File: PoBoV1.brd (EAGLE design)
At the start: 142.2 x 64.8 mm, 80 parts, among them IC1 INA232, Q1 IPZ40N04S5L-4R8, Q2 IPZ40N04S5L-4R8, U1 TPS55288RPMR, X1 +Vin, X18 OUT, X19 ADDRSEL, X3 SDA, X4 SCL, X5 VOUT/EXT, X6 FB SEL, X7 EN SEL, X8 MODE SEL

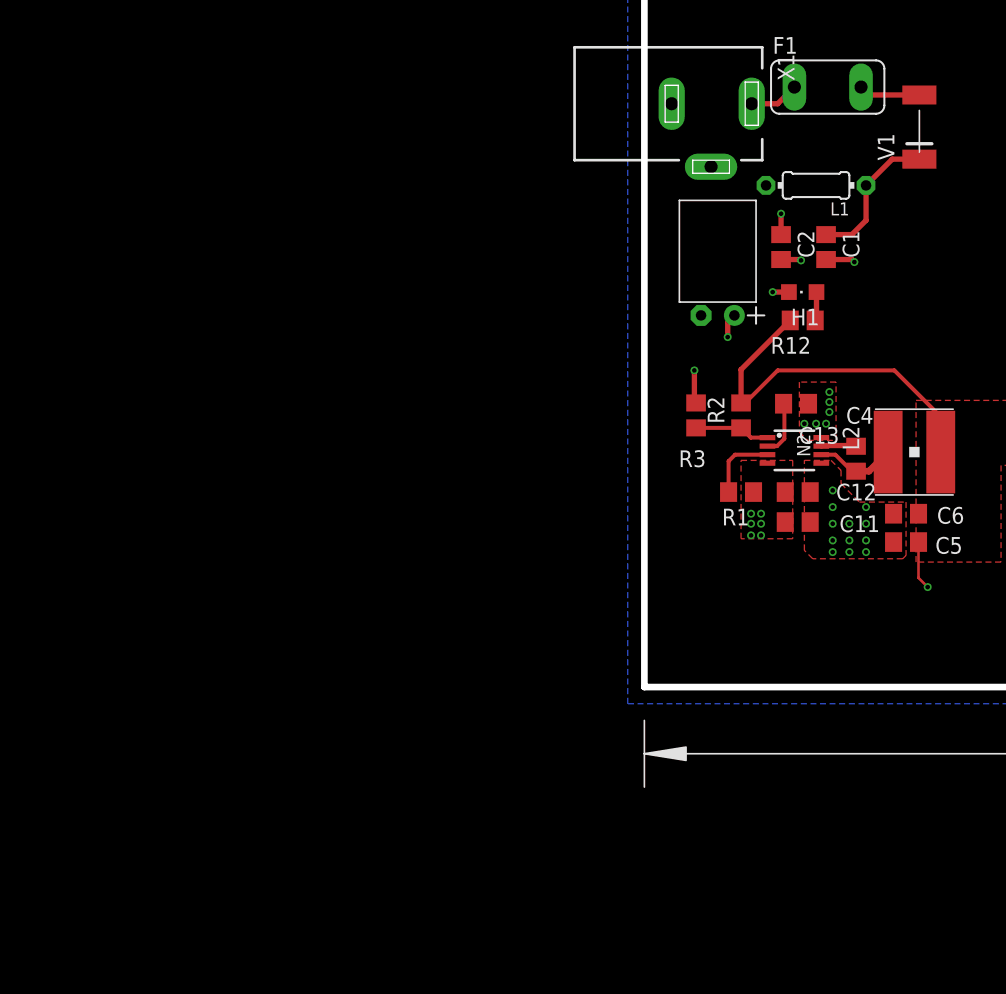
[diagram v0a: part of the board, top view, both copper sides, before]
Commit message: Made some traces thiccer and added bananaplug
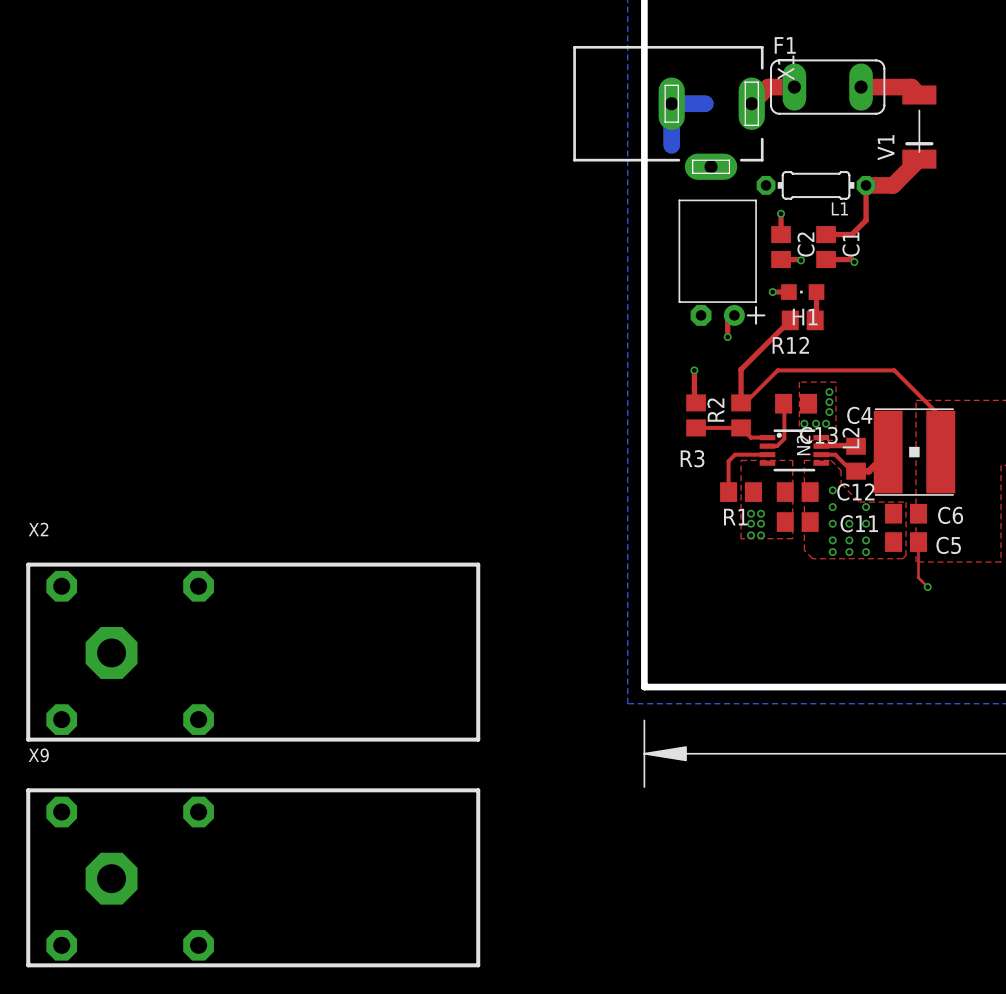
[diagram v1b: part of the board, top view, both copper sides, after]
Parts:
- added X2: BANANAJACKBANANAJACK-BLACK, con_PoeD:BANANAJACK
- added X9: BANANAJACKBANANAJACK-RED, con_PoeD:BANANAJACK
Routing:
- net PGND: track 11.5 -> 17.3 mm
- net VCC: track 7.47 -> 9.60 mm
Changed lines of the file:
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@@
 <setting verticaltext="up"/>
 </settings>
-<grid distance="0.1" unitdist="mm" unit="mm" style="lines" multiple="1" display="no" altdistance="5" altunitdist="mil" altunit="mil"/>
+<grid distance="3.93700787" unitdist="mil" unit="mil" style="lines" multiple="1" display="no" altdistance="5" altunitdist="mil" altunit="mil"/>
 <layers>
 <layer number="1" name="Top" color="4" fill="1" visible="yes" active="yes"/>
@@
 <layer number="23" name="tOrigins" color="15" fill="1" visible="yes" active="yes"/>
 <layer number="24" name="bOrigins" color="15" fill="1" visible="yes" active="yes"/>
-<layer number="25" name="tNames" color="7" fill="1" visible="no" active="yes"/>
-<layer number="26" name="bNames" color="7" fill="1" visible="no" active="yes"/>
-<layer number="27" name="tValues" color="7" fill="1" visible="no" active="yes"/>
-<layer number="28" name="bValues" color="7" fill="1" visible="no" active="yes"/>
+<layer number="25" name="tNames" color="7" fill="1" visible="yes" active="yes"/>
+<layer number="26" name="bNames" color="7" fill="1" visible="yes" active="yes"/>
+<layer number="27" name="tValues" color="7" fill="1" visible="yes" active="yes"/>
+<layer number="28" name="bValues" color="7" fill="1" visible="yes" active="yes"/>
 <layer number="29" name="tStop" color="18" fill="3" visible="no" active="yes"/>
 <layer number="30" name="bStop" color="18" fill="5" visible="no" active="yes"/>
@@
 </layers>
 <board>
-<fusionsync huburn="a.YnVzaW5lc3M6aHRsc2FsemJ1cmc0OTQ" projecturn="a.YnVzaW5lc3M6aHRsc2FsemJ1cmc0OTQjRDIwMjIwOTIyNTU5MzQ0OTgx" f3durn="urn:adsk.wipprod:dm.lineage:csbvKVBoTdiHW0NaQc5oYw" pcbguid="" lastpulledtime="" lastsyncedchangeguid="" latestrevisionid="9871288b-a15c-4ba2-ae32-102903a1a666" lastsyncedrevisionid="9871288b-a15c-4ba2-ae32-102903a1a666" lastboardhashguid="696e8a89-2363-cbe4-064f-950dd3bf885a" lastpushedtime="2024-12-28T18:32:02Z" linktopcb3d="true"/>
+<fusionsync huburn="a.YnVzaW5lc3M6aHRsc2FsemJ1cmc0OTQ" projecturn="a.YnVzaW5lc3M6aHRsc2FsemJ1cmc0OTQjRDIwMjIwOTIyNTU5MzQ0OTgx" f3durn="urn:adsk.wipprod:dm.lineage:csbvKVBoTdiHW0NaQc5oYw" pcbguid="" lastpulledtime="" lastsyncedchangeguid="" latestrevisionid="9871288b-a15c-4ba2-ae32-102903a1a666" lastsyncedrevisionid="9871288b-a15c-4ba2-ae32-102903a1a666" lastboardhashguid="696e8a89-2363-cbe4-064f-950dd3bf885a" lastpushedtime="2024-12-28T18:32:02Z" linktopcb3d="false"/>
 <plain>
 <wire x1="0" y1="0" x2="0" y2="64.77" width="0.508" layer="20"/>
@@
 <element name="FABRICATION" library="fabrication" package="FABRIACTION" value="" x="39.12" y="-10" smashed="yes"/>
 <element name="BOM" library="fabrication" package="BOM" value="" x="0.15" y="-0.15" smashed="yes"/>
+<element name="X2" library="con_PoeD" library_urn="urn:adsk.eagle:library:37347325" package="BANANAJACK" package3d_urn="urn:adsk.eagle:package:40115465/7" value="BANANAJACKBANANAJACK-BLACK" x="-40.6" y="2.6" smashed="yes">
+<attribute name="NAME" x="-46.95" y="11.49" size="1.016" layer="25"/>
+<attribute name="VALUE" x="-46.95" y="10.22" size="0.8128" layer="27"/>
+</element>
+<element name="X9" library="con_PoeD" library_urn="urn:adsk.eagle:library:37347325" package="BANANAJACK" package3d_urn="urn:adsk.eagle:package:40115465/7" value="BANANAJACKBANANAJACK-RED" x="-40.6" y="-14.6" smashed="yes">
+<attribute name="NAME" x="-46.95" y="-5.71" size="1.016" layer="25"/>
+<attribute name="VALUE" x="-46.95" y="-6.98" size="0.8128" layer="27"/>
+</element>
 </elements>
 <signals>
@@
 <wire x1="106.553" y1="10.988" x2="105.664" y2="10.099" width="0.2032" layer="1"/>
 <wire x1="105.664" y1="10.099" x2="105.664" y2="9.398" width="0.2032" layer="1"/>
-<polygon width="0.1524" layer="2">
+<polygon width="0.1524" layer="2" isolate="0.3048">
 <vertex x="-1.27" y="71.12"/>
 <vertex x="147.32" y="71.12"/>
@@
 <contactref element="C10" pad="2"/>
 <contactref element="H1" pad="C"/>
-<polygon width="0.4064" layer="16">
+<polygon width="0.4064" layer="16" isolate="0.3048">
 <vertex x="-1.27" y="67.31"/>
 <vertex x="144.78" y="67.31"/>
@@
 <via x="111.76" y="52.07" extent="1-16" drill="0.35"/>
 <via x="113.03" y="52.07" extent="1-16" drill="0.35"/>
+<wire x1="2.08" y1="44.45" x2="4.65" y2="44.45" width="1.27" layer="16"/>
+<wire x1="2.08" y1="44.45" x2="2.08" y2="41.28" width="1.27" layer="16"/>
 </signal>
 <signal name="N$20">
@@
 <contactref element="C1" pad="1"/>
 <contactref element="L1" pad="1"/>
-<wire x1="20.955" y1="40.227" x2="18.891" y2="40.227" width="0.4064" layer="1"/>
-<wire x1="18.891" y1="40.227" x2="16.891" y2="38.227" width="0.4064" layer="1"/>
 <wire x1="16.891" y1="38.227" x2="16.891" y2="35.56" width="0.4064" layer="1"/>
 <wire x1="15.809" y1="34.478" x2="13.843" y2="34.478" width="0.4064" layer="1"/>
 <wire x1="16.891" y1="35.56" x2="15.809" y2="34.478" width="0.4064" layer="1"/>
+<wire x1="20.955" y1="40.227" x2="18.955" y2="38.227" width="1.27" layer="1"/>
+<wire x1="18.955" y1="38.227" x2="16.891" y2="38.227" width="1.27" layer="1"/>
 </signal>
 <signal name="N$29">
@@
 <vertex x="7.366" y="11.303"/>
 </polygon>
-<polygon width="0.2032" layer="15">
+<polygon width="1.27" layer="15" isolate="0.3048">
 <vertex x="-1.27" y="66.04"/>
 <vertex x="144.78" y="66.04"/>
@@
 <wire x1="113.411" y1="12.634" x2="113.411" y2="11.43" width="0.2032" layer="1"/>
 <via x="113.411" y="11.43" extent="1-16" drill="0.35"/>
+<wire x1="9.271" y1="38.227" x2="9.244" y2="38.2" width="1.27" layer="15"/>
+<wire x1="9.271" y1="38.227" x2="9.271" y2="36.129" width="1.27" layer="15"/>
 </signal>
 <signal name="BOOT1">
@@
 <contactref element="X1" pad="1"/>
 <contactref element="F1" pad="1"/>
-<wire x1="11.43" y1="45.72" x2="10.16" y2="44.45" width="0.4064" layer="1"/>
-<wire x1="8.18" y1="44.45" x2="10.16" y2="44.45" width="0.4064" layer="1"/>
+<wire x1="8.18" y1="44.45" x2="9.45" y2="45.72" width="1.27" layer="1"/>
+<wire x1="9.45" y1="45.72" x2="11.43" y2="45.72" width="1.27" layer="1"/>
 </signal>
 <signal name="N$22">
 <contactref element="V1" pad="A"/>
 <contactref element="F1" pad="2"/>
-<wire x1="20.955" y1="45.117" x2="17.113" y2="45.117" width="0.4064" layer="1"/>
-<wire x1="16.51" y1="45.72" x2="17.113" y2="45.117" width="0.4064" layer="1"/>
+<wire x1="16.51" y1="45.72" x2="20.352" y2="45.72" width="1.27" layer="1"/>
+<wire x1="20.352" y1="45.72" x2="20.955" y2="45.117" width="1.27" layer="1"/>
 </signal>
 </signals>

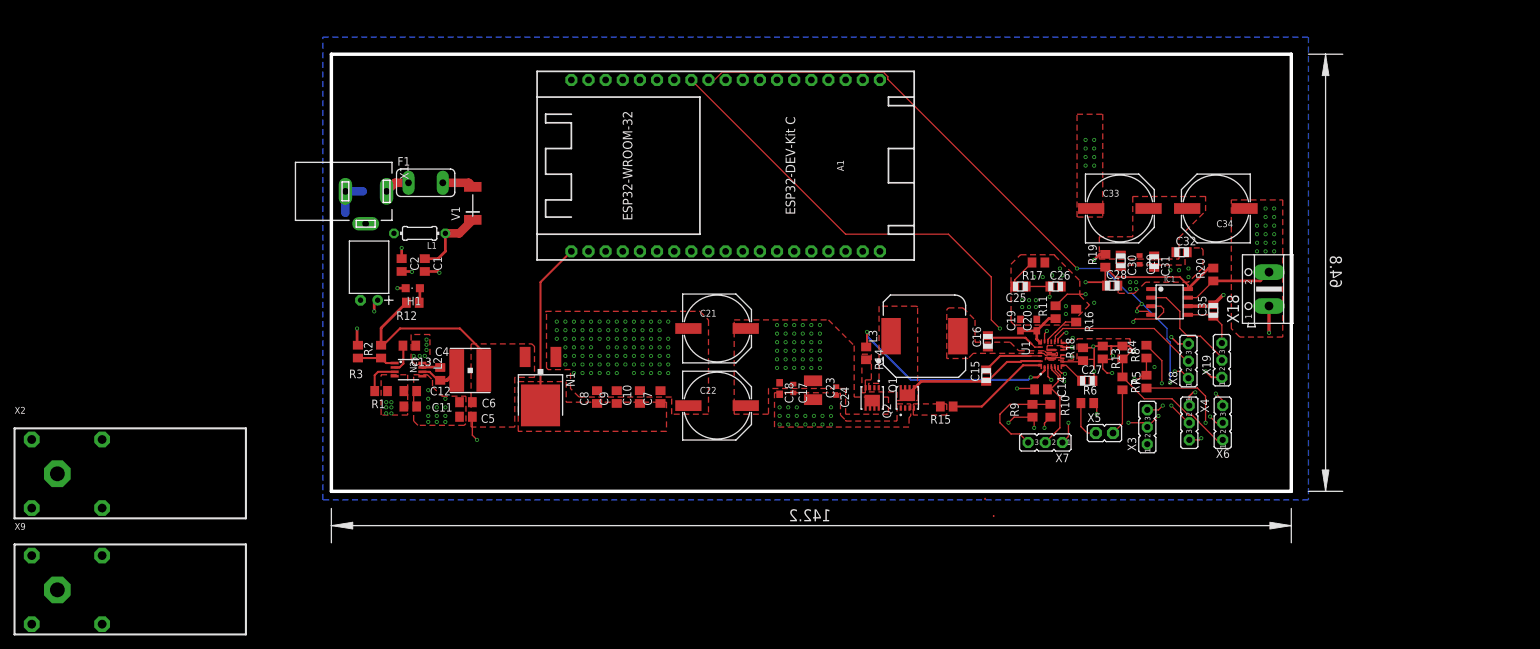
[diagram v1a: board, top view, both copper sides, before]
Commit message: Add files via upload
Added testpoints and banana jacks
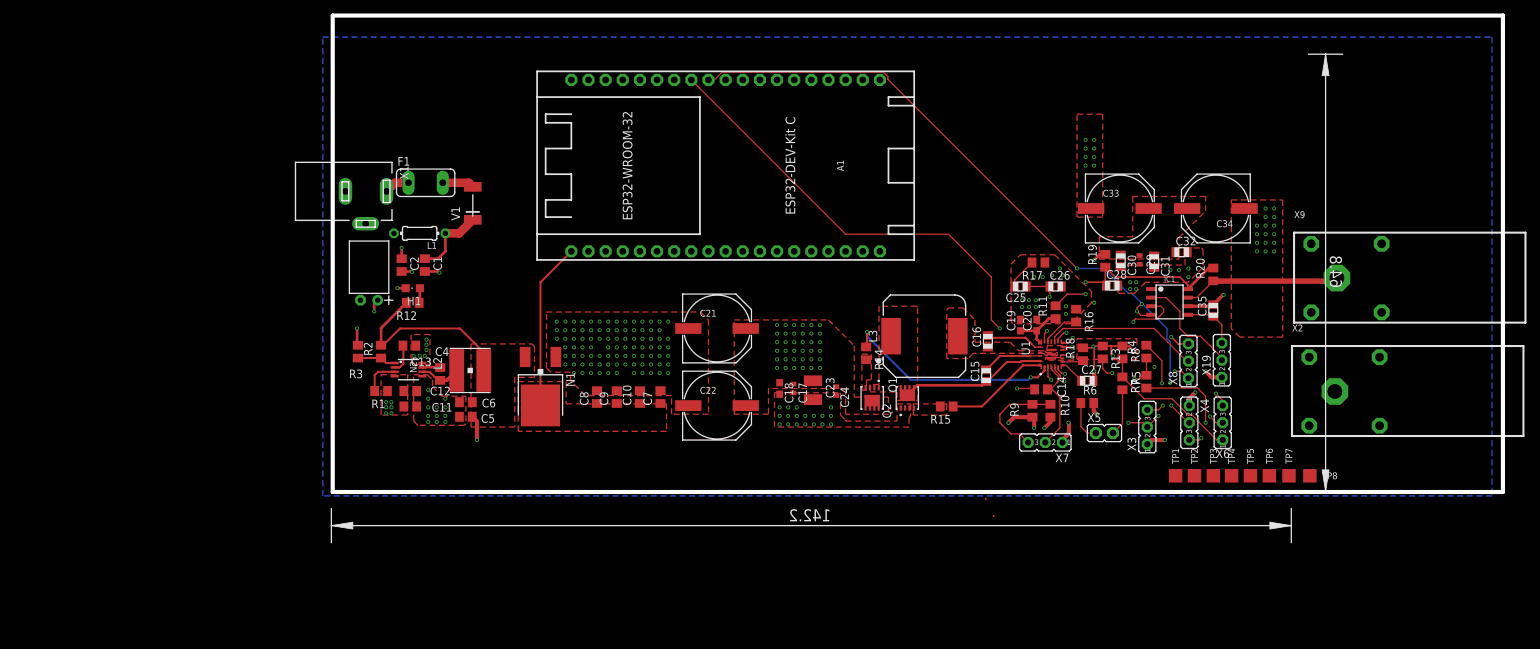
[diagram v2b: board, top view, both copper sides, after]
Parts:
- removed X18: OUT, con_SekS:AK500/2
- added TP1, TP2, TP3, TP4, TP5, TP6, TP7, TP8: TPP-SMD-20SN, testpoint:SMD-20SN
- moved X9 195.1 mm to (149.0, 31.6)
- moved X2 189.7 mm to (148.7, 14.8)
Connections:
- removed net N$21: IC1.7, R20.1, X18.2
- new net VOUT: IC1.7, R20.1, TP7.TP, X9.P$1
- net BOOT1: now also TP1.TP
- net BOOT2: now also TP2.TP
- net PGND: now also TP5.TP, X2.P$1; no longer X18.1
- net SCL: now also TP8.TP
- net SDA: now also TP6.TP
- net SW1: now also TP3.TP
- net SW2: now also TP4.TP
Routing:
- net VOUT: track 0.00 -> 23.3 mm
- net N$21: track 13.6 -> 0.00 mm
- net PGND: track 17.3 -> 7.56 mm, vias 163 -> 162
- net GND: track 36.8 -> 39.4 mm, vias 25 -> 26
- net VCC: track 9.60 -> 7.47 mm
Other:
- board size 142.2 x 64.8 mm -> 173.4 x 70.6 mm

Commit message: Fixed routing, connected testpoints
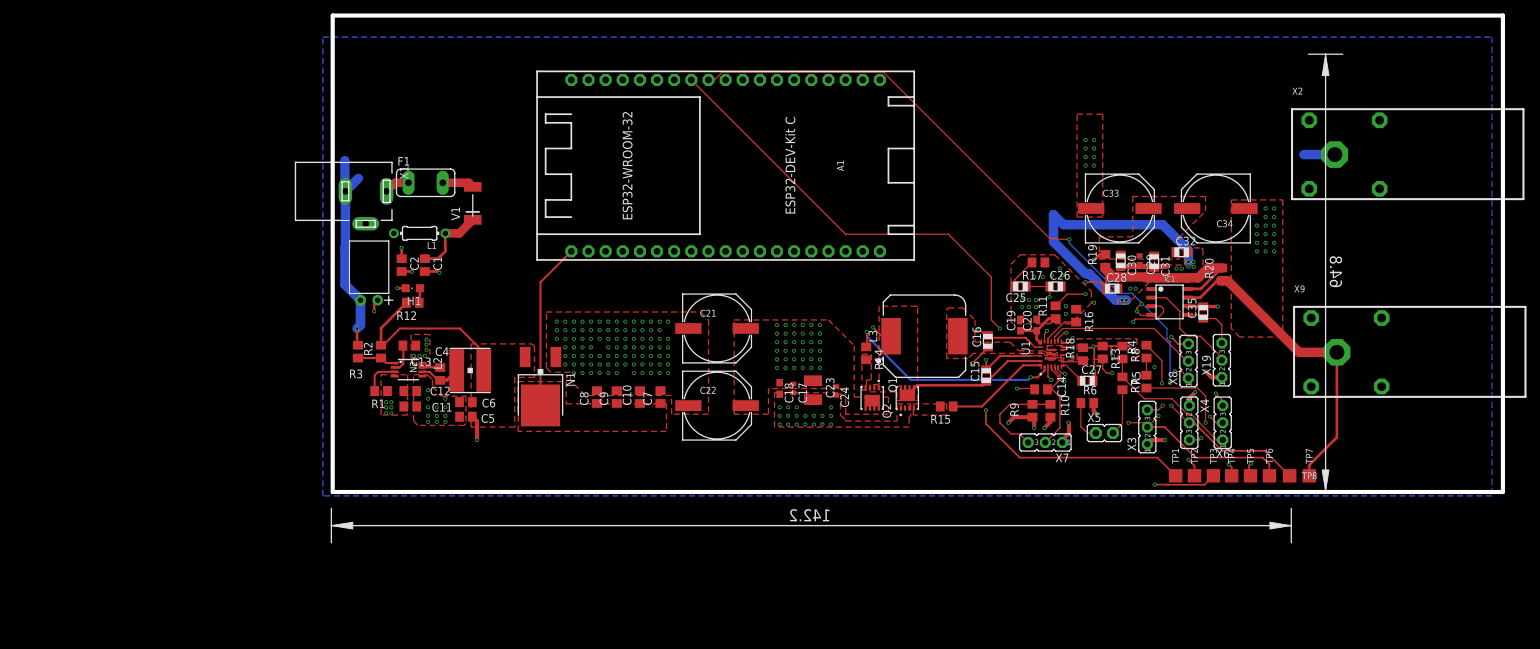
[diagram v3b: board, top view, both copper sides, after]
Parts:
- moved X2 35.1 mm to (148.7, 49.9)
- moved X9 11.0 mm to (149.0, 20.6)
- moved TP7 3.00 mm to (144.9, 2.30)
- moved TP8 3.00 mm to (142.0, 2.30)
- moved C35 1.52 mm to (129.2, 26.5)
- moved R20 1.31 mm to (132.0, 32.1)
- moved C28 0.44 mm to (115.7, 30.0)
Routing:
- net PGND: track 7.56 -> 92.1 mm, vias 162 -> 165
- net SW1: track 21.8 -> 93.6 mm, vias 0 -> 2
- net SW2: track 0.00 -> 54.7 mm, vias 0 -> 2
- net BOOT2: track 8.49 -> 60.3 mm, vias 0 -> 2
- net BOOT1: track 8.86 -> 51.1 mm, vias 0 -> 2
- net VOUT: track 23.3 -> 47.5 mm
- net SDA: track 119.8 -> 141.9 mm
- net SCL: track 126.9 -> 145.2 mm
- net ISN: track 36.6 -> 43.4 mm
- net GND: track 39.4 -> 38.0 mm
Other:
- board text added: "BOOT1"
- board text added: "BOOT2"
- board text added: "PGND"
- board text added: "SCL"
- board text added: "SDA"
- board text added: "SW1"
- board text added: "VOUT"
